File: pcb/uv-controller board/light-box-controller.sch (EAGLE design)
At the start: 31 parts, among them IC1 LDL112D33R, J1 12 VIN, J2 UVLED-OUT, Q1 FQP30N06L, U1 L7805, U2 ESP-WROOM-32

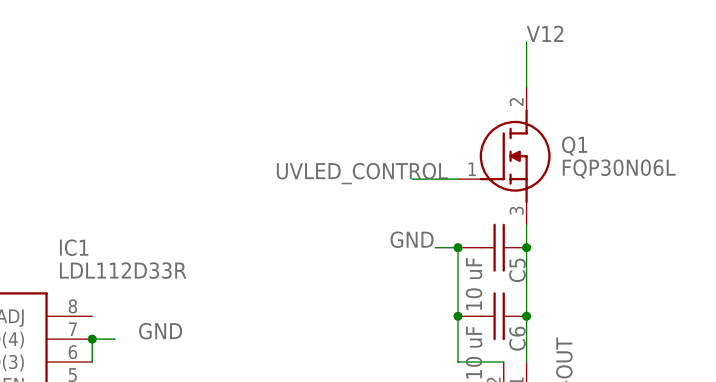
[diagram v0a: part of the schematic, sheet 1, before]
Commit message: added pull down resisitor
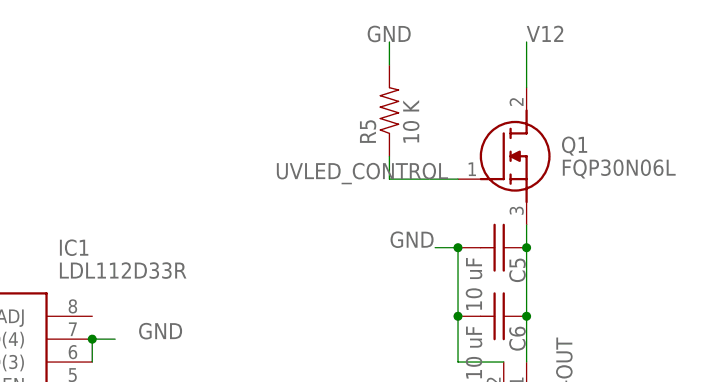
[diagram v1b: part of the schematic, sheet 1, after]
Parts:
- added R5: 10 K, passives:RESISTOR0805-RES
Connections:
- net GND: now also R5.2
- net UVLED_CONTROL: now also R5.1
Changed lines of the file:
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@@
 <part name="C13" library="passives" deviceset="C-US" device="C0805K" package3d_urn="urn:adsk.eagle:package:8089589/1" value="0.1 uF"/>
 <part name="J3" library="connector" deviceset="M09" device="LONGPADS"/>
+<part name="R5" library="passives" deviceset="RESISTOR" device="0805-RES" value="10 K"/>
 </parts>
 <sheets>
@@
 <attribute name="NAME" x="94.996" y="41.275" size="1.778" layer="95"/>
 <attribute name="VALUE" x="94.996" y="36.449" size="1.778" layer="96"/>
+</instance>
+<instance part="R5" gate="G$1" x="149.86" y="81.28" smashed="yes" rot="R90">
+<attribute name="NAME" x="148.3614" y="77.47" size="1.778" layer="95" rot="R90"/>
+<attribute name="VALUE" x="153.162" y="77.47" size="1.778" layer="96" rot="R90"/>
 </instance>
 </instances>
@@
 <label x="149.86" y="66.04" size="1.778" layer="95"/>
 </segment>
+<segment>
+<pinref part="R5" gate="G$1" pin="2"/>
+<wire x1="149.86" y1="86.36" x2="149.86" y2="88.9" width="0.1524" layer="91"/>
+<label x="147.32" y="88.9" size="1.778" layer="95"/>
+</segment>
 </net>
 <net name="UVLED_CONTROL" class="0">
 <segment>
 <pinref part="Q1" gate="G$1" pin="G"/>
-<wire x1="157.48" y1="73.66" x2="152.4" y2="73.66" width="0.1524" layer="91"/>
+<wire x1="157.48" y1="73.66" x2="149.86" y2="73.66" width="0.1524" layer="91"/>
 <label x="137.16" y="73.66" size="1.778" layer="95"/>
-</segment>
-</net>
+<pinref part="R5" gate="G$1" pin="1"/>
+<wire x1="149.86" y1="76.2" x2="149.86" y2="73.66" width="0.1524" layer="91"/>
+</segment>
+</net>

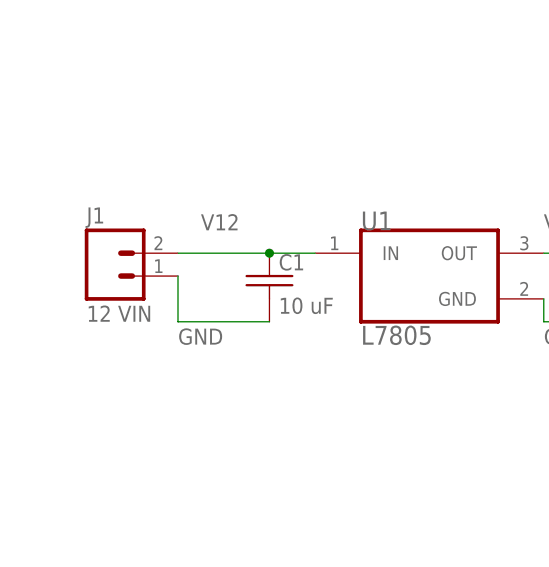
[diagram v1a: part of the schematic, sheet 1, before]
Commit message: update to use ground planes
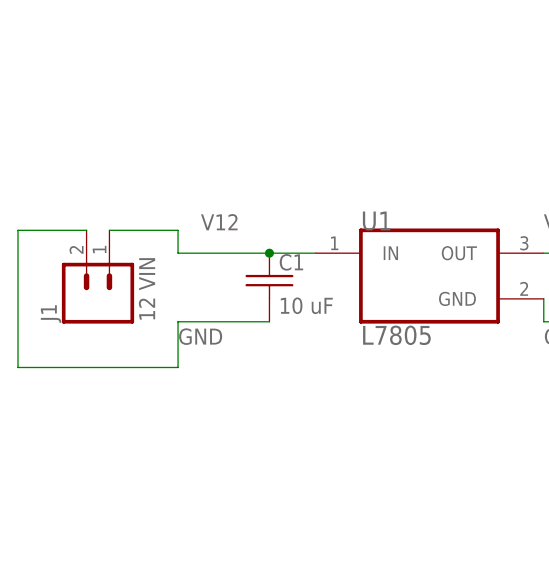
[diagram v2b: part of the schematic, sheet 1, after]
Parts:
- J1, J2: device connector:M023.5MM -> connector:M025MM
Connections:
- net GND: now also J1.2; no longer J1.1
- net V12: now also J1.1; no longer J1.2
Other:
- moved on the sheet: J1

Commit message: moving away from IO15 as I'm pretty sure its messing up the touch screen
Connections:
- net TOUCH_DATA_OUT: now also U2.IO22; no longer U2.IO15
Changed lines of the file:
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@@
 <grid distance="0.1" unitdist="inch" unit="inch" style="lines" multiple="1" display="no" altdistance="0.01" altunitdist="inch" altunit="inch"/>
 <layers>
-<layer number="1" name="Top" color="4" fill="1" visible="yes" active="no"/>
-<layer number="2" name="Route2" color="16" fill="1" visible="yes" active="no"/>
-<layer number="3" name="Route3" color="17" fill="1" visible="yes" active="no"/>
-<layer number="4" name="Route4" color="18" fill="1" visible="yes" active="no"/>
-<layer number="5" name="Route5" color="19" fill="1" visible="yes" active="no"/>
-<layer number="6" name="Route6" color="25" fill="1" visible="yes" active="no"/>
-<layer number="7" name="Route7" color="26" fill="1" visible="yes" active="no"/>
-<layer number="8" name="Route8" color="27" fill="1" visible="yes" active="no"/>
-<layer number="9" name="Route9" color="28" fill="1" visible="yes" active="no"/>
-<layer number="10" name="Route10" color="29" fill="1" visible="yes" active="no"/>
-<layer number="11" name="Route11" color="30" fill="1" visible="yes" active="no"/>
-<layer number="12" name="Route12" color="20" fill="1" visible="yes" active="no"/>
-<layer number="13" name="Route13" color="21" fill="1" visible="yes" active="no"/>
-<layer number="14" name="Route14" color="22" fill="1" visible="yes" active="no"/>
-<layer number="15" name="Route15" color="23" fill="1" visible="yes" active="no"/>
-<layer number="16" name="Bottom" color="1" fill="1" visible="yes" active="no"/>
-<layer number="17" name="Pads" color="2" fill="1" visible="yes" active="no"/>
-<layer number="18" name="Vias" color="2" fill="1" visible="yes" active="no"/>
-<layer number="19" name="Unrouted" color="6" fill="1" visible="yes" active="no"/>
-<layer number="20" name="Dimension" color="24" fill="1" visible="yes" active="no"/>
-<layer number="21" name="tPlace" color="7" fill="1" visible="yes" active="no"/>
-<layer number="22" name="bPlace" color="7" fill="1" visible="yes" active="no"/>
-<layer number="23" name="tOrigins" color="15" fill="1" visible="yes" active="no"/>
-<layer number="24" name="bOrigins" color="15" fill="1" visible="yes" active="no"/>
-<layer number="25" name="tNames" color="7" fill="1" visible="yes" active="no"/>
-<layer number="26" name="bNames" color="7" fill="1" visible="yes" active="no"/>
-<layer number="27" name="tValues" color="7" fill="1" visible="yes" active="no"/>
-<layer number="28" name="bValues" color="7" fill="1" visible="yes" active="no"/>
+<layer number="1" name="Top" color="4" fill="1" visible="no" active="no"/>
+<layer number="2" name="Route2" color="16" fill="1" visible="no" active="no"/>
+<layer number="3" name="Route3" color="17" fill="1" visible="no" active="no"/>
+<layer number="4" name="Route4" color="18" fill="1" visible="no" active="no"/>
+<layer number="5" name="Route5" color="19" fill="1" visible="no" active="no"/>
+<layer number="6" name="Route6" color="25" fill="1" visible="no" active="no"/>
+<layer number="7" name="Route7" color="26" fill="1" visible="no" active="no"/>
+<layer number="8" name="Route8" color="27" fill="1" visible="no" active="no"/>
+<layer number="9" name="Route9" color="28" fill="1" visible="no" active="no"/>
+<layer number="10" name="Route10" color="29" fill="1" visible="no" active="no"/>
+<layer number="11" name="Route11" color="30" fill="1" visible="no" active="no"/>
+<layer number="12" name="Route12" color="20" fill="1" visible="no" active="no"/>
+<layer number="13" name="Route13" color="21" fill="1" visible="no" active="no"/>
+<layer number="14" name="Route14" color="22" fill="1" visible="no" active="no"/>
+<layer number="15" name="Route15" color="23" fill="1" visible="no" active="no"/>
+<layer number="16" name="Bottom" color="1" fill="1" visible="no" active="no"/>
+<layer number="17" name="Pads" color="2" fill="1" visible="no" active="no"/>
+<layer number="18" name="Vias" color="2" fill="1" visible="no" active="no"/>
+<layer number="19" name="Unrouted" color="6" fill="1" visible="no" active="no"/>
+<layer number="20" name="Dimension" color="24" fill="1" visible="no" active="no"/>
+<layer number="21" name="tPlace" color="7" fill="1" visible="no" active="no"/>
+<layer number="22" name="bPlace" color="7" fill="1" visible="no" active="no"/>
+<layer number="23" name="tOrigins" color="15" fill="1" visible="no" active="no"/>
+<layer number="24" name="bOrigins" color="15" fill="1" visible="no" active="no"/>
+<layer number="25" name="tNames" color="7" fill="1" visible="no" active="no"/>
+<layer number="26" name="bNames" color="7" fill="1" visible="no" active="no"/>
+<layer number="27" name="tValues" color="7" fill="1" visible="no" active="no"/>
+<layer number="28" name="bValues" color="7" fill="1" visible="no" active="no"/>
 <layer number="29" name="tStop" color="7" fill="3" visible="no" active="no"/>
 <layer number="30" name="bStop" color="7" fill="6" visible="no" active="no"/>
@@
 <layer number="35" name="tGlue" color="7" fill="4" visible="no" active="no"/>
 <layer number="36" name="bGlue" color="7" fill="5" visible="no" active="no"/>
-<layer number="37" name="tTest" color="7" fill="1" visible="yes" active="no"/>
-<layer number="38" name="bTest" color="7" fill="1" visible="yes" active="no"/>
+<layer number="37" name="tTest" color="7" fill="1" visible="no" active="no"/>
+<layer number="38" name="bTest" color="7" fill="1" visible="no" active="no"/>
 <layer number="39" name="tKeepout" color="4" fill="11" visible="no" active="no"/>
 <layer number="40" name="bKeepout" color="1" fill="11" visible="no" active="no"/>
@@
 <layer number="44" name="Drills" color="7" fill="1" visible="no" active="no"/>
 <layer number="45" name="Holes" color="7" fill="1" visible="no" active="no"/>
-<layer number="46" name="Milling" color="3" fill="1" visible="yes" active="no"/>
-<layer number="47" name="Measures" color="7" fill="1" visible="yes" active="no"/>
-<layer number="48" name="Document" color="7" fill="1" visible="yes" active="no"/>
-<layer number="49" name="Reference" color="7" fill="1" visible="yes" active="no"/>
-<layer number="50" name="dxf" color="7" fill="1" visible="yes" active="no"/>
-<layer number="51" name="tDocu" color="7" fill="1" visible="yes" active="no"/>
-<layer number="52" name="bDocu" color="7" fill="1" visible="yes" active="no"/>
-<layer number="53" name="tGND_GNDA" color="7" fill="9" visible="yes" active="no"/>
-<layer number="54" name="bGND_GNDA" color="1" fill="9" visible="yes" active="no"/>
-<layer number="56" name="wert" color="7" fill="1" visible="yes" active="no"/>
-<layer number="57" name="tCAD" color="7" fill="1" visible="yes" active="no"/>
-<layer number="59" name="tCarbon" color="7" fill="1" visible="yes" active="no"/>
-<layer number="60" name="bCarbon" color="7" fill="1" visible="yes" active="no"/>
+<layer number="46" name="Milling" color="3" fill="1" visible="no" active="no"/>
+<layer number="47" name="Measures" color="7" fill="1" visible="no" active="no"/>
+<layer number="48" name="Document" color="7" fill="1" visible="no" active="no"/>
+<layer number="49" name="Reference" color="7" fill="1" visible="no" active="no"/>
+<layer number="50" name="dxf" color="7" fill="1" visible="no" active="no"/>
+<layer number="51" name="tDocu" color="7" fill="1" visible="no" active="no"/>
+<layer number="52" name="bDocu" color="7" fill="1" visible="no" active="no"/>
+<layer number="53" name="tGND_GNDA" color="7" fill="9" visible="no" active="no"/>
+<layer number="54" name="bGND_GNDA" color="1" fill="9" visible="no" active="no"/>
+<layer number="56" name="wert" color="7" fill="1" visible="no" active="no"/>
+<layer number="57" name="tCAD" color="7" fill="1" visible="no" active="no"/>
+<layer number="59" name="tCarbon" color="7" fill="1" visible="no" active="no"/>
+<layer number="60" name="bCarbon" color="7" fill="1" visible="no" active="no"/>
 <layer number="88" name="SimResults" color="9" fill="1" visible="yes" active="yes"/>
 <layer number="89" name="SimProbes" color="9" fill="1" visible="yes" active="yes"/>
@@
 </segment>
 <segment>
-<pinref part="U2" gate="G$1" pin="IO15"/>
-<wire x1="81.28" y1="25.4" x2="81.28" y2="22.86" width="0.1524" layer="91"/>
-<label x="81.28" y="2.54" size="1.778" layer="95" rot="R90"/>
-</segment>
-</net>
+<pinref part="U2" gate="G$1" pin="IO22"/>
+<wire x1="96.52" y1="63.5" x2="99.06" y2="63.5" width="0.1524" layer="91"/>
+<label x="99.06" y="63.5" size="1.778" layer="95"/>
+</segment>
+</net>

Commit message: added notes to ensure I don't mess up the n-channel mosfet again.  :)
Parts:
- added U$4: CMD_C0DE_LOGOCMD_CODE_LOGO_SILK, logos:CMD_C0DE_LOGOCMD_CODE_LOGO_SILK
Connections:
- removed net N$12: C5.1, C6.1, J2.1, Q1.S
- new net N$2: J2.2, Q1.D
- net GND: now also Q1.S; no longer J2.2
- net V12: now also C5.1, C6.1, J2.1; no longer Q1.D
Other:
- note added: "For N-Channel mosfets power flows from drain TO source. So we want to make souce connected to ground and drain connect to power. Most of the time we'll want power to start from power source to circuit (load) through MOSFET to source to ground."
- moved on the sheet: Q1, R5
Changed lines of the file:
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@@
 <part name="J3" library="connector" deviceset="M09" device="LONGPADS"/>
 <part name="R5" library="passives" deviceset="RESISTOR" device="0805-RES" value="10 K"/>
+<part name="U$4" library="logos" deviceset="CMD_C0DE_LOGO" device="CMD_CODE_LOGO_SILK"/>
 </parts>
 <sheets>
 <sheet>
 <plain>
+<text x="134.62" y="22.86" size="1.778" layer="91">For N-Channel mosfets power flows from drain TO source.
+So we want to make souce connected to ground and drain
+connect to power.  Most of the time we'll want power to start
+from power source to circuit (load) through MOSFET to source to ground.</text>
 </plain>
 <instances>
-<instance part="Q1" gate="G$1" x="157.48" y="73.66" smashed="yes">
-<attribute name="NAME" x="168.91" y="77.47" size="1.778" layer="95" align="center-left"/>
-<attribute name="VALUE" x="168.91" y="74.93" size="1.778" layer="96" align="center-left"/>
+<instance part="Q1" gate="G$1" x="149.86" y="76.2" smashed="yes">
+<attribute name="NAME" x="161.29" y="80.01" size="1.778" layer="95" align="center-left"/>
+<attribute name="VALUE" x="161.29" y="77.47" size="1.778" layer="96" align="center-left"/>
 </instance>
 <instance part="U1" gate="G$1" x="53.34" y="48.26" smashed="yes">
@@
 <attribute name="VALUE" x="94.996" y="36.449" size="1.778" layer="96"/>
 </instance>
-<instance part="R5" gate="G$1" x="149.86" y="81.28" smashed="yes" rot="R90">
-<attribute name="NAME" x="148.3614" y="77.47" size="1.778" layer="95" rot="R90"/>
-<attribute name="VALUE" x="153.162" y="77.47" size="1.778" layer="96" rot="R90"/>
-</instance>
+<instance part="R5" gate="G$1" x="142.24" y="83.82" smashed="yes" rot="R90">
+<attribute name="NAME" x="140.7414" y="80.01" size="1.778" layer="95" rot="R90"/>
+<attribute name="VALUE" x="145.542" y="80.01" size="1.778" layer="96" rot="R90"/>
+</instance>
+<instance part="U$4" gate="G$1" x="55.88" y="25.4" smashed="yes"/>
 </instances>
 <busses>
@@
 </segment>
 <segment>
-<pinref part="Q1" gate="G$1" pin="D"/>
-<wire x1="165.1" y1="83.82" x2="165.1" y2="88.9" width="0.1524" layer="91"/>
-<label x="165.1" y="88.9" size="1.778" layer="95"/>
+<pinref part="J2" gate="G$1" pin="1"/>
+<wire x1="165.1" y1="53.34" x2="165.1" y2="58.42" width="0.1524" layer="91"/>
+<pinref part="C5" gate="G$1" pin="1"/>
+<wire x1="165.1" y1="58.42" x2="165.1" y2="66.04" width="0.1524" layer="91"/>
+<pinref part="C6" gate="G$1" pin="1"/>
+<junction x="165.1" y="58.42"/>
+<wire x1="165.1" y1="66.04" x2="165.1" y2="86.36" width="0.1524" layer="91"/>
+<junction x="165.1" y="66.04"/>
+<label x="167.64" y="86.36" size="1.778" layer="95"/>
 </segment>
 </net>
@@
 </segment>
 <segment>
-<pinref part="J2" gate="G$1" pin="2"/>
-<wire x1="162.56" y1="53.34" x2="157.48" y2="53.34" width="0.1524" layer="91"/>
 <pinref part="C6" gate="G$1" pin="2"/>
-<wire x1="157.48" y1="53.34" x2="157.48" y2="58.42" width="0.1524" layer="91"/>
 <pinref part="C5" gate="G$1" pin="2"/>
 <wire x1="157.48" y1="58.42" x2="157.48" y2="66.04" width="0.1524" layer="91"/>
-<junction x="157.48" y="58.42"/>
 <wire x1="157.48" y1="66.04" x2="154.94" y2="66.04" width="0.1524" layer="91"/>
 <junction x="157.48" y="66.04"/>
 <label x="149.86" y="66.04" size="1.778" layer="95"/>
+<pinref part="Q1" gate="G$1" pin="S"/>
+<wire x1="157.48" y1="66.04" x2="157.48" y2="71.12" width="0.1524" layer="91"/>
 </segment>
 <segment>
 <pinref part="R5" gate="G$1" pin="2"/>
-<wire x1="149.86" y1="86.36" x2="149.86" y2="88.9" width="0.1524" layer="91"/>
-<label x="147.32" y="88.9" size="1.778" layer="95"/>
+<wire x1="142.24" y1="88.9" x2="142.24" y2="91.44" width="0.1524" layer="91"/>
+<label x="139.7" y="91.44" size="1.778" layer="95"/>
 </segment>
 </net>
@@
 <segment>
 <pinref part="Q1" gate="G$1" pin="G"/>
-<wire x1="157.48" y1="73.66" x2="149.86" y2="73.66" width="0.1524" layer="91"/>
-<label x="137.16" y="73.66" size="1.778" layer="95"/>
+<wire x1="149.86" y1="76.2" x2="142.24" y2="76.2" width="0.1524" layer="91"/>
+<label x="129.54" y="76.2" size="1.778" layer="95"/>
 <pinref part="R5" gate="G$1" pin="1"/>
-<wire x1="149.86" y1="76.2" x2="149.86" y2="73.66" width="0.1524" layer="91"/>
-</segment>
-</net>
-<net name="N$12" class="0">
-<segment>
-<pinref part="Q1" gate="G$1" pin="S"/>
-<pinref part="J2" gate="G$1" pin="1"/>
-<wire x1="165.1" y1="53.34" x2="165.1" y2="58.42" width="0.1524" layer="91"/>
-<pinref part="C5" gate="G$1" pin="1"/>
-<wire x1="165.1" y1="58.42" x2="165.1" y2="66.04" width="0.1524" layer="91"/>
-<wire x1="165.1" y1="66.04" x2="165.1" y2="68.58" width="0.1524" layer="91"/>
-<junction x="165.1" y="66.04"/>
-<pinref part="C6" gate="G$1" pin="1"/>
-<junction x="165.1" y="58.42"/>
+<wire x1="142.24" y1="78.74" x2="142.24" y2="76.2" width="0.1524" layer="91"/>
+</segment>
+</net>
+<net name="N$2" class="0">
+<segment>
+<pinref part="J2" gate="G$1" pin="2"/>
+<wire x1="162.56" y1="53.34" x2="154.94" y2="53.34" width="0.1524" layer="91"/>
+<wire x1="154.94" y1="53.34" x2="154.94" y2="35.56" width="0.1524" layer="91"/>
+<wire x1="154.94" y1="35.56" x2="180.34" y2="35.56" width="0.1524" layer="91"/>
+<wire x1="180.34" y1="35.56" x2="180.34" y2="93.98" width="0.1524" layer="91"/>
+<wire x1="180.34" y1="93.98" x2="157.48" y2="93.98" width="0.1524" layer="91"/>
+<pinref part="Q1" gate="G$1" pin="D"/>
+<wire x1="157.48" y1="93.98" x2="157.48" y2="86.36" width="0.1524" layer="91"/>
 </segment>
 </net>
@@
 </drawing>
 <compatibility>
+<note version="6.3" minversion="6.2.2" severity="warning">
+Since Version 6.2.2 text objects can contain more than one line,
+which will not be processed correctly with this version.
+</note>
 <note version="8.3" severity="warning">
 Since Version 8.3, EAGLE supports URNs for individual library
